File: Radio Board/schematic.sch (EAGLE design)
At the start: 8 parts, among them J1 132134RP

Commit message: added a 100uF cap
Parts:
- added C3: 08054W107MAT2A, 08054W107MAT2A:08054W107MAT2A
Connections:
- net 3V3.2: now also C3.2
- net GND: now also C3.1
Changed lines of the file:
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@@
 <part name="SUPPLY3" library="supply2" library_urn="urn:adsk.eagle:library:372" deviceset="GND" device=""/>
 <part name="SUPPLY1" library="supply2" library_urn="urn:adsk.eagle:library:372" deviceset="GND" device=""/>
+<part name="C3" library="08054W107MAT2A" deviceset="08054W107MAT2A" device=""/>
 </parts>
 <sheets>
@@
 <attribute name="VALUE" x="71.755" y="19.685" size="1.778" layer="96"/>
 </instance>
+<instance part="C3" gate="G$1" x="-2.54" y="60.96" smashed="yes" rot="R90">
+<attribute name="NAME" x="-8.89" y="69.85" size="1.778" layer="95" rot="R90" align="center-left"/>
+<attribute name="VALUE" x="-6.35" y="69.85" size="1.778" layer="96" rot="R90" align="center-left"/>
+</instance>
 </instances>
 <busses>
@@
 <junction x="10.16" y="71.12"/>
 <label x="10.16" y="76.2" size="1.778" layer="95"/>
+<pinref part="C3" gate="G$1" pin="2"/>
+<wire x1="-2.54" y1="73.66" x2="5.08" y2="73.66" width="0.1524" layer="91"/>
+<wire x1="5.08" y1="73.66" x2="5.08" y2="71.12" width="0.1524" layer="91"/>
+<junction x="5.08" y="71.12"/>
 </segment>
 <segment>
@@
 <wire x1="15.24" y1="63.5" x2="10.16" y2="63.5" width="0.1524" layer="91"/>
 <junction x="10.16" y="63.5"/>
+<pinref part="C3" gate="G$1" pin="1"/>
+<wire x1="-2.54" y1="60.96" x2="5.08" y2="60.96" width="0.1524" layer="91"/>
+<wire x1="5.08" y1="60.96" x2="5.08" y2="63.5" width="0.1524" layer="91"/>
+<junction x="5.08" y="63.5"/>
 </segment>
 <segment>

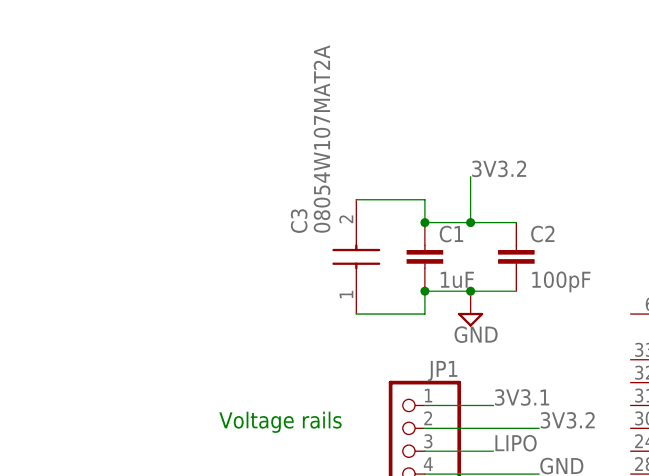
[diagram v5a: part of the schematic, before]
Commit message: updated radio
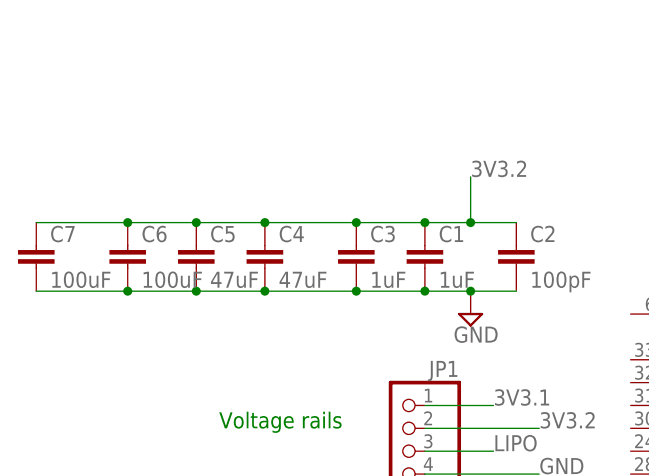
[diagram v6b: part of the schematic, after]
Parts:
- added C4, C5: 47uF, SparkFun-Retired:2.2UF-CERCAP-10009
- added C6, C7: 100uF, SparkFun-Retired:2.2UF-CERCAP-10009
- C1: device SparkFun-Capacitors:0.1UF-0603-100V-10% -> SparkFun-Retired:2.2UF-CERCAP-10009
- C3: value 08054W107MAT2A -> 1uF; device 08054W107MAT2A:08054W107MAT2A -> SparkFun-Retired:2.2UF-CERCAP-10009
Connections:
- net 3V3.2: now also C3.1, C4.1, C5.1, C6.1, C7.1; no longer C3.2
- net GND: now also C3.2, C4.2, C5.2, C6.2, C7.2; no longer C3.1
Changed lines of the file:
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@@
 <part name="GPS" library="SparkFun-Connectors" deviceset="CONN_10" device="NO_SILK_PTH_FEMALE"/>
 <part name="J3" library="SparkFun-Connectors" deviceset="CONN_10" device="NO_SILK_PTH_FEMALE"/>
-<part name="C1" library="SparkFun-Capacitors" deviceset="0.1UF" device="-0603-100V-10%" value="1uF"/>
 <part name="C2" library="SparkFun-Capacitors" deviceset="0.1UF" device="-0603-100V-10%" value="100pF"/>
 <part name="SUPPLY2" library="supply2" library_urn="urn:adsk.eagle:library:372" deviceset="GND" device=""/>
@@
 <part name="SUPPLY3" library="supply2" library_urn="urn:adsk.eagle:library:372" deviceset="GND" device=""/>
 <part name="SUPPLY1" library="supply2" library_urn="urn:adsk.eagle:library:372" deviceset="GND" device=""/>
-<part name="C3" library="08054W107MAT2A" deviceset="08054W107MAT2A" device=""/>
+<part name="C3" library="SparkFun-Retired" deviceset="2.2UF-CER" device="CAP-10009" value="1uF"/>
+<part name="C4" library="SparkFun-Retired" deviceset="2.2UF-CER" device="CAP-10009" value="47uF"/>
+<part name="C5" library="SparkFun-Retired" deviceset="2.2UF-CER" device="CAP-10009" value="47uF"/>
+<part name="C6" library="SparkFun-Retired" deviceset="2.2UF-CER" device="CAP-10009" value="100uF"/>
+<part name="C7" library="SparkFun-Retired" deviceset="2.2UF-CER" device="CAP-10009" value="100uF"/>
+<part name="C1" library="SparkFun-Retired" deviceset="2.2UF-CER" device="CAP-10009" value="1uF"/>
 </parts>
 <sheets>
@@
 <attribute name="NAME" x="76.2" y="-15.748" size="1.778" layer="95" font="vector" rot="R180"/>
 </instance>
-<instance part="C1" gate="G$1" x="5.08" y="66.04" smashed="yes">
-<attribute name="NAME" x="6.604" y="68.961" size="1.778" layer="95" font="vector"/>
-<attribute name="VALUE" x="6.604" y="63.881" size="1.778" layer="96" font="vector"/>
-</instance>
 <instance part="C2" gate="G$1" x="15.24" y="66.04" smashed="yes">
 <attribute name="NAME" x="16.764" y="68.961" size="1.778" layer="95" font="vector"/>
@@
 <attribute name="VALUE" x="71.755" y="19.685" size="1.778" layer="96"/>
 </instance>
-<instance part="C3" gate="G$1" x="-2.54" y="60.96" smashed="yes" rot="R90">
-<attribute name="NAME" x="-8.89" y="69.85" size="1.778" layer="95" rot="R90" align="center-left"/>
-<attribute name="VALUE" x="-6.35" y="69.85" size="1.778" layer="96" rot="R90" align="center-left"/>
+<instance part="C3" gate="G$1" x="-2.54" y="66.04" smashed="yes">
+<attribute name="NAME" x="-1.016" y="68.961" size="1.778" layer="95"/>
+<attribute name="VALUE" x="-1.016" y="63.881" size="1.778" layer="96"/>
+</instance>
+<instance part="C4" gate="G$1" x="-12.7" y="66.04" smashed="yes">
+<attribute name="NAME" x="-11.176" y="68.961" size="1.778" layer="95"/>
+<attribute name="VALUE" x="-11.176" y="63.881" size="1.778" layer="96"/>
+</instance>
+<instance part="C5" gate="G$1" x="-20.32" y="66.04" smashed="yes">
+<attribute name="NAME" x="-18.796" y="68.961" size="1.778" layer="95"/>
+<attribute name="VALUE" x="-18.796" y="63.881" size="1.778" layer="96"/>
+</instance>
+<instance part="C6" gate="G$1" x="-27.94" y="66.04" smashed="yes">
+<attribute name="NAME" x="-26.416" y="68.961" size="1.778" layer="95"/>
+<attribute name="VALUE" x="-26.416" y="63.881" size="1.778" layer="96"/>
+</instance>
+<instance part="C7" gate="G$1" x="-38.1" y="66.04" smashed="yes">
+<attribute name="NAME" x="-36.576" y="68.961" size="1.778" layer="95"/>
+<attribute name="VALUE" x="-36.576" y="63.881" size="1.778" layer="96"/>
+</instance>
+<instance part="C1" gate="G$1" x="5.08" y="66.04" smashed="yes">
+<attribute name="NAME" x="6.604" y="68.961" size="1.778" layer="95"/>
+<attribute name="VALUE" x="6.604" y="63.881" size="1.778" layer="96"/>
 </instance>
 </instances>
@@
 <segment>
 <wire x1="10.16" y1="76.2" x2="10.16" y2="71.12" width="0.1524" layer="91"/>
-<pinref part="C1" gate="G$1" pin="1"/>
-<wire x1="5.08" y1="71.12" x2="10.16" y2="71.12" width="0.1524" layer="91"/>
 <pinref part="C2" gate="G$1" pin="1"/>
 <wire x1="15.24" y1="71.12" x2="10.16" y2="71.12" width="0.1524" layer="91"/>
 <junction x="10.16" y="71.12"/>
 <label x="10.16" y="76.2" size="1.778" layer="95"/>
-<pinref part="C3" gate="G$1" pin="2"/>
-<wire x1="-2.54" y1="73.66" x2="5.08" y2="73.66" width="0.1524" layer="91"/>
-<wire x1="5.08" y1="73.66" x2="5.08" y2="71.12" width="0.1524" layer="91"/>
+<pinref part="C7" gate="G$1" pin="1"/>
+<wire x1="10.16" y1="71.12" x2="5.08" y2="71.12" width="0.1524" layer="91"/>
+<pinref part="C3" gate="G$1" pin="1"/>
+<wire x1="5.08" y1="71.12" x2="-2.54" y2="71.12" width="0.1524" layer="91"/>
+<wire x1="-2.54" y1="71.12" x2="-12.7" y2="71.12" width="0.1524" layer="91"/>
+<junction x="-2.54" y="71.12"/>
+<pinref part="C4" gate="G$1" pin="1"/>
+<wire x1="-12.7" y1="71.12" x2="-20.32" y2="71.12" width="0.1524" layer="91"/>
+<junction x="-12.7" y="71.12"/>
+<pinref part="C5" gate="G$1" pin="1"/>
+<wire x1="-20.32" y1="71.12" x2="-27.94" y2="71.12" width="0.1524" layer="91"/>
+<junction x="-20.32" y="71.12"/>
+<pinref part="C6" gate="G$1" pin="1"/>
+<wire x1="-27.94" y1="71.12" x2="-38.1" y2="71.12" width="0.1524" layer="91"/>
+<junction x="-27.94" y="71.12"/>
+<pinref part="C1" gate="G$1" pin="1"/>
 <junction x="5.08" y="71.12"/>
 </segment>
@@
 </segment>
 <segment>
-<pinref part="C1" gate="G$1" pin="2"/>
 <pinref part="SUPPLY2" gate="GND" pin="GND"/>
-<wire x1="5.08" y1="63.5" x2="10.16" y2="63.5" width="0.1524" layer="91"/>
 <pinref part="C2" gate="G$1" pin="2"/>
 <wire x1="15.24" y1="63.5" x2="10.16" y2="63.5" width="0.1524" layer="91"/>
 <junction x="10.16" y="63.5"/>
-<pinref part="C3" gate="G$1" pin="1"/>
-<wire x1="-2.54" y1="60.96" x2="5.08" y2="60.96" width="0.1524" layer="91"/>
-<wire x1="5.08" y1="60.96" x2="5.08" y2="63.5" width="0.1524" layer="91"/>
+<pinref part="C7" gate="G$1" pin="2"/>
+<wire x1="-38.1" y1="63.5" x2="-27.94" y2="63.5" width="0.1524" layer="91"/>
+<pinref part="C3" gate="G$1" pin="2"/>
+<wire x1="-27.94" y1="63.5" x2="-20.32" y2="63.5" width="0.1524" layer="91"/>
+<wire x1="-20.32" y1="63.5" x2="-12.7" y2="63.5" width="0.1524" layer="91"/>
+<wire x1="-12.7" y1="63.5" x2="-2.54" y2="63.5" width="0.1524" layer="91"/>
+<wire x1="-2.54" y1="63.5" x2="5.08" y2="63.5" width="0.1524" layer="91"/>
+<junction x="-2.54" y="63.5"/>
+<pinref part="C4" gate="G$1" pin="2"/>
+<junction x="-12.7" y="63.5"/>
+<pinref part="C5" gate="G$1" pin="2"/>
+<junction x="-20.32" y="63.5"/>
+<pinref part="C6" gate="G$1" pin="2"/>
+<junction x="-27.94" y="63.5"/>
+<pinref part="C1" gate="G$1" pin="2"/>
+<wire x1="5.08" y1="63.5" x2="10.16" y2="63.5" width="0.1524" layer="91"/>
 <junction x="5.08" y="63.5"/>
 </segment>

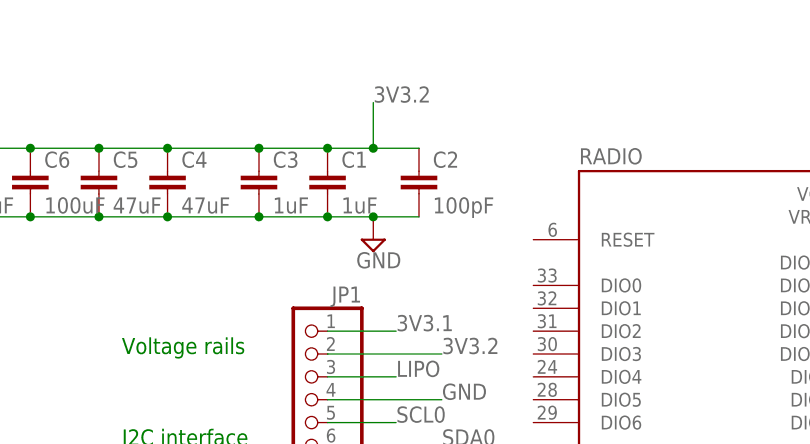
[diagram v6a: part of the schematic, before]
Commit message: Radio Board - Routed traces, missing ground plane
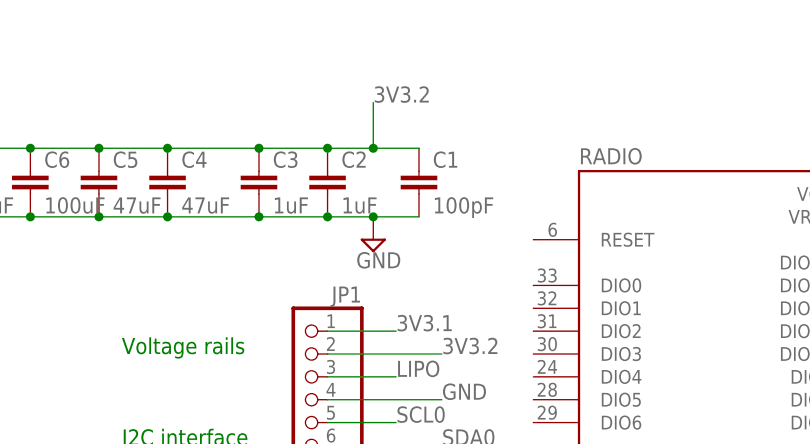
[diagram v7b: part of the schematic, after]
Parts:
- C1: value 1uF -> 100pF; device SparkFun-Retired:2.2UF-CERCAP-10009 -> SparkFun-Capacitors:0.1UF-0603-100V-10%
- C2: value 100pF -> 1uF; device SparkFun-Capacitors:0.1UF-0603-100V-10% -> SparkFun-Retired:2.2UF-CERCAP-10009
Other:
- moved on the sheet: C1, C2
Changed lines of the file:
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@@
 <part name="GPS" library="SparkFun-Connectors" deviceset="CONN_10" device="NO_SILK_PTH_FEMALE"/>
 <part name="J3" library="SparkFun-Connectors" deviceset="CONN_10" device="NO_SILK_PTH_FEMALE"/>
-<part name="C2" library="SparkFun-Capacitors" deviceset="0.1UF" device="-0603-100V-10%" value="100pF"/>
+<part name="C1" library="SparkFun-Capacitors" deviceset="0.1UF" device="-0603-100V-10%" value="100pF"/>
 <part name="SUPPLY2" library="supply2" library_urn="urn:adsk.eagle:library:372" deviceset="GND" device=""/>
 <part name="RADIO" library="XBP9X-DMRS-001" deviceset="XBP9X-DMRS-001" device=""/>
@@
 <part name="C6" library="SparkFun-Retired" deviceset="2.2UF-CER" device="CAP-10009" value="100uF"/>
 <part name="C7" library="SparkFun-Retired" deviceset="2.2UF-CER" device="CAP-10009" value="100uF"/>
-<part name="C1" library="SparkFun-Retired" deviceset="2.2UF-CER" device="CAP-10009" value="1uF"/>
+<part name="C2" library="SparkFun-Retired" deviceset="2.2UF-CER" device="CAP-10009" value="1uF"/>
 </parts>
 <sheets>
@@
 <attribute name="NAME" x="76.2" y="-15.748" size="1.778" layer="95" font="vector" rot="R180"/>
 </instance>
-<instance part="C2" gate="G$1" x="15.24" y="66.04" smashed="yes">
+<instance part="C1" gate="G$1" x="15.24" y="66.04" smashed="yes">
 <attribute name="NAME" x="16.764" y="68.961" size="1.778" layer="95" font="vector"/>
 <attribute name="VALUE" x="16.764" y="63.881" size="1.778" layer="96" font="vector"/>
@@
 <attribute name="VALUE" x="-36.576" y="63.881" size="1.778" layer="96"/>
 </instance>
-<instance part="C1" gate="G$1" x="5.08" y="66.04" smashed="yes">
+<instance part="C2" gate="G$1" x="5.08" y="66.04" smashed="yes">
 <attribute name="NAME" x="6.604" y="68.961" size="1.778" layer="95"/>
 <attribute name="VALUE" x="6.604" y="63.881" size="1.778" layer="96"/>
@@
 <segment>
 <wire x1="10.16" y1="76.2" x2="10.16" y2="71.12" width="0.1524" layer="91"/>
-<pinref part="C2" gate="G$1" pin="1"/>
+<pinref part="C1" gate="G$1" pin="1"/>
 <wire x1="15.24" y1="71.12" x2="10.16" y2="71.12" width="0.1524" layer="91"/>
 <junction x="10.16" y="71.12"/>
@@
 <wire x1="-27.94" y1="71.12" x2="-38.1" y2="71.12" width="0.1524" layer="91"/>
 <junction x="-27.94" y="71.12"/>
-<pinref part="C1" gate="G$1" pin="1"/>
+<pinref part="C2" gate="G$1" pin="1"/>
 <junction x="5.08" y="71.12"/>
 </segment>
@@
 <segment>
 <pinref part="SUPPLY2" gate="GND" pin="GND"/>
-<pinref part="C2" gate="G$1" pin="2"/>
+<pinref part="C1" gate="G$1" pin="2"/>
 <wire x1="15.24" y1="63.5" x2="10.16" y2="63.5" width="0.1524" layer="91"/>
 <junction x="10.16" y="63.5"/>
@@
 <pinref part="C6" gate="G$1" pin="2"/>
 <junction x="-27.94" y="63.5"/>
-<pinref part="C1" gate="G$1" pin="2"/>
+<pinref part="C2" gate="G$1" pin="2"/>
 <wire x1="5.08" y1="63.5" x2="10.16" y2="63.5" width="0.1524" layer="91"/>
 <junction x="5.08" y="63.5"/>
